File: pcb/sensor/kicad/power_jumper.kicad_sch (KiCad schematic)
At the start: 5 parts, among them J1 FPC 6P 0.5 mm

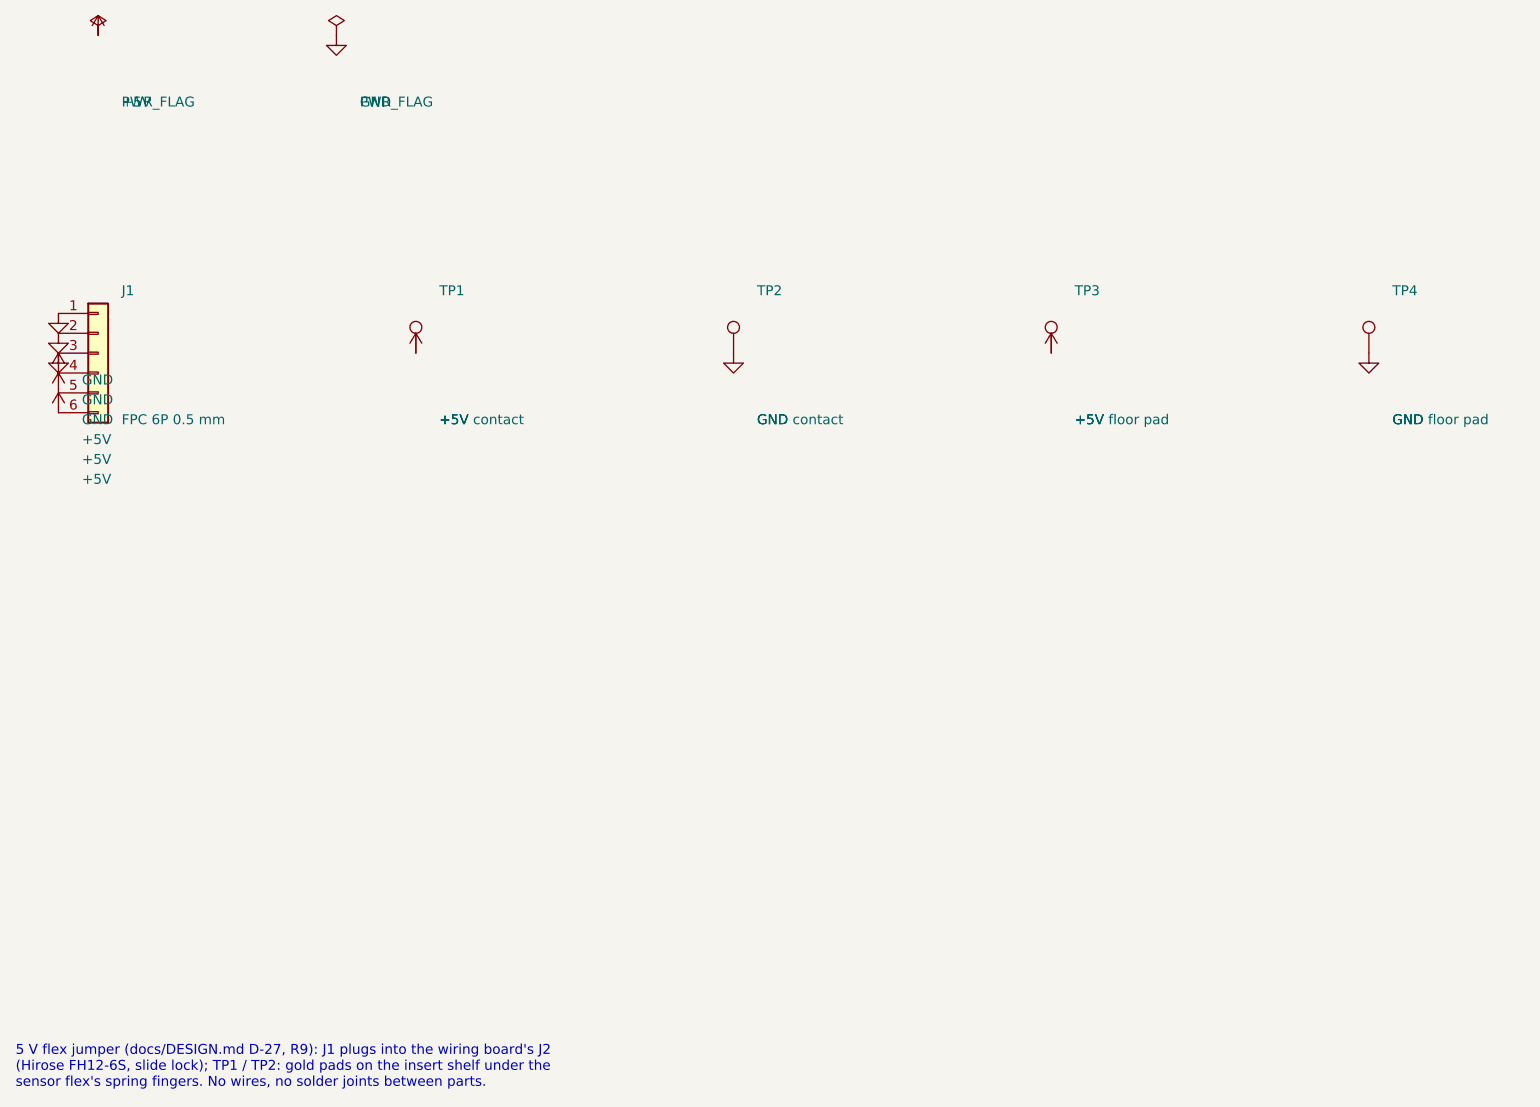
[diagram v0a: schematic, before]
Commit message: Smaller plate, flex ramps and tape points, battery-free tongue on the sensor flex, back cover hooks
- Plate 72 x 132, 5 V contact in the corner, band groove, microphone below the band, two-layer
  sensor flex (D-47)
- Ramps over the flex slopes; tape geometry and tape renders (render_tape.py, D-48)
- Battery-free tongue moved from the 5 V jumper to the sensor flex: under the trim's tab and strip,
  under the floor insert, which hangs from the strip; EU tongue under its floor insert (D-49)
- Back cover: bottom latch 2.9 mm from the edge, end-section snap hooks, notch for the run under
  the GND block; plate clips kept for PETG
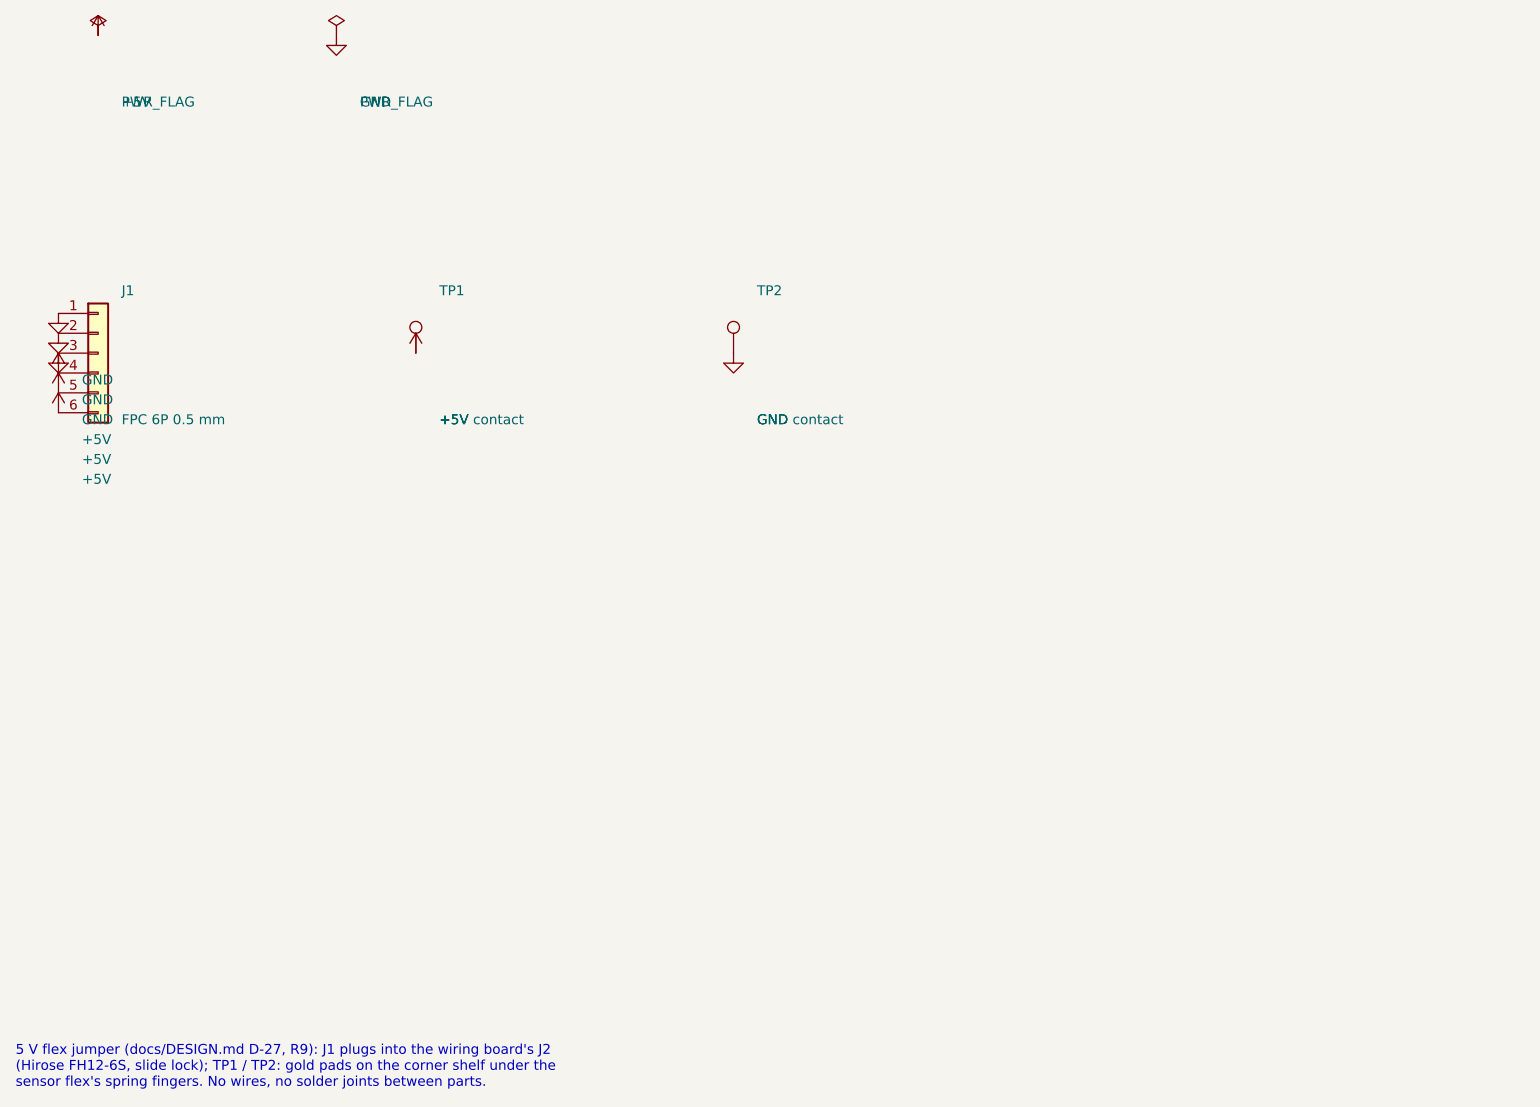
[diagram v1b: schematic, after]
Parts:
- removed TP3: +5V floor pad, sensor:Contact_Pad_7x4mm, symbol sensor:TestPoint
- removed TP4: GND floor pad, sensor:Contact_Pad_7x4mm, symbol sensor:TestPoint
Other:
- note added: "5 V flex jumper (docs/DESIGN.md D-27, R9): J1 plugs into the wiring board's J2 (Hirose FH12-6S, slide lock); TP1 / TP2: gold pads on the corner shelf under the sensor flex's spring fingers. No wires, no solder joints between parts."
- note removed: "5 V flex jumper (docs/DESIGN.md D-27, R9): J1 plugs into the wiring board's J2 (Hirose FH12-6S, slide lock); TP1 / TP2: gold pads on the insert shelf under the sensor flex's spring fingers. No wires, no solder joints between parts."
